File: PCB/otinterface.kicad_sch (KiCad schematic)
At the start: 43 parts, among them K1 G6K-2, Q1 BC857C, Q10 BC847C, Q11 BC857C, Q12 BC847C, Q2 BC847C, Q4 BC857C, Q5 BC857C, Q6 BC857C, Q7 BC857C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

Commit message: finish 45/24
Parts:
- K1: value G6K-2 -> G6K-2F-Y-5V; LCSC C47190 -> C2982926
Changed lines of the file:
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@@
 	(wire
 		(pts
-			(xy 193.04 88.9) (xy 220.98 88.9)
+			(xy 199.39 88.9) (xy 220.98 88.9)
 		)
 		(stroke
@@
 	(wire
 		(pts
-			(xy 193.04 92.71) (xy 175.26 92.71)
+			(xy 199.39 92.71) (xy 175.26 92.71)
 		)
 		(stroke
@@
 	(wire
 		(pts
-			(xy 193.04 88.9) (xy 193.04 92.71)
+			(xy 199.39 88.9) (xy 199.39 92.71)
 		)
 		(stroke
@@
 			)
 		)
-		(property "Value" "G6K-2"
+		(property "Value" "G6K-2F-Y-5V"
 			(at 167.64 85.09 90)
 			(effects
@@
 			)
 		)
-		(property "LCSC" "C47190"
+		(property "LCSC" "C2982926"
 			(at 167.64 102.87 0)
 			(effects

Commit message: add pullups for stability
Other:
- company: (none) -> Seegel Systeme
- title: (none) -> OT Thing
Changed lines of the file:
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@@
 	(generator_version "8.0")
 	(paper "A4")
+	(title_block
+		(title "OT Thing")
+		(date "2025-01-08")
+		(rev "2/25")
+		(company "Seegel Systeme")
+	)
 	(junction
 		(at 187.96 102.87)

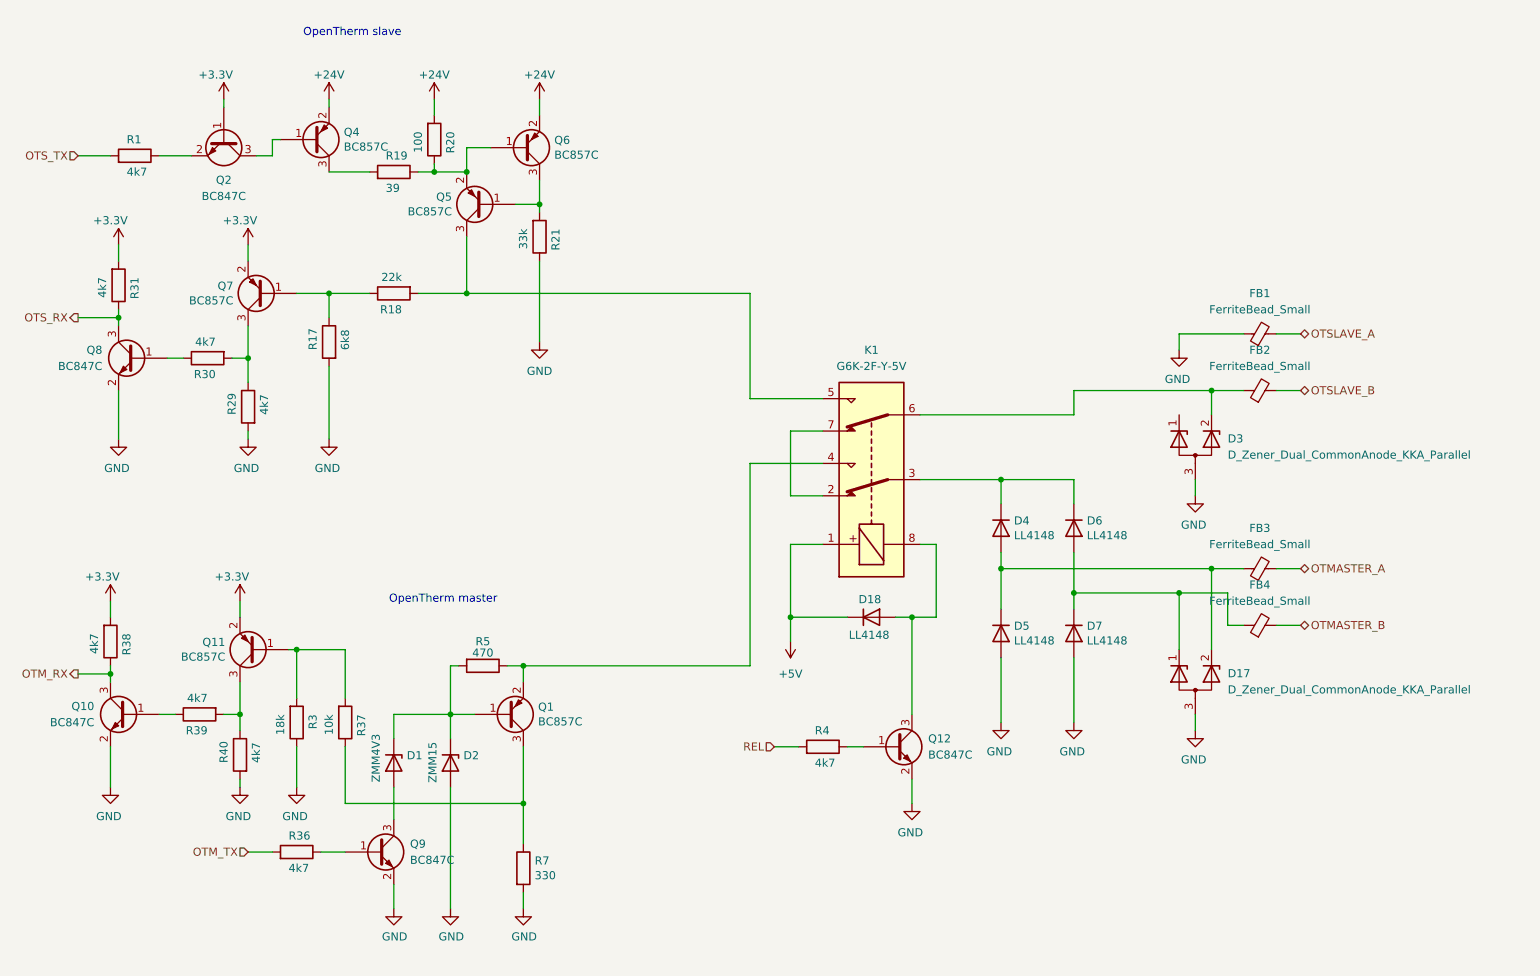
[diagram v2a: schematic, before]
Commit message: migrate to pioarduino smart power add more OT values new partitiontable
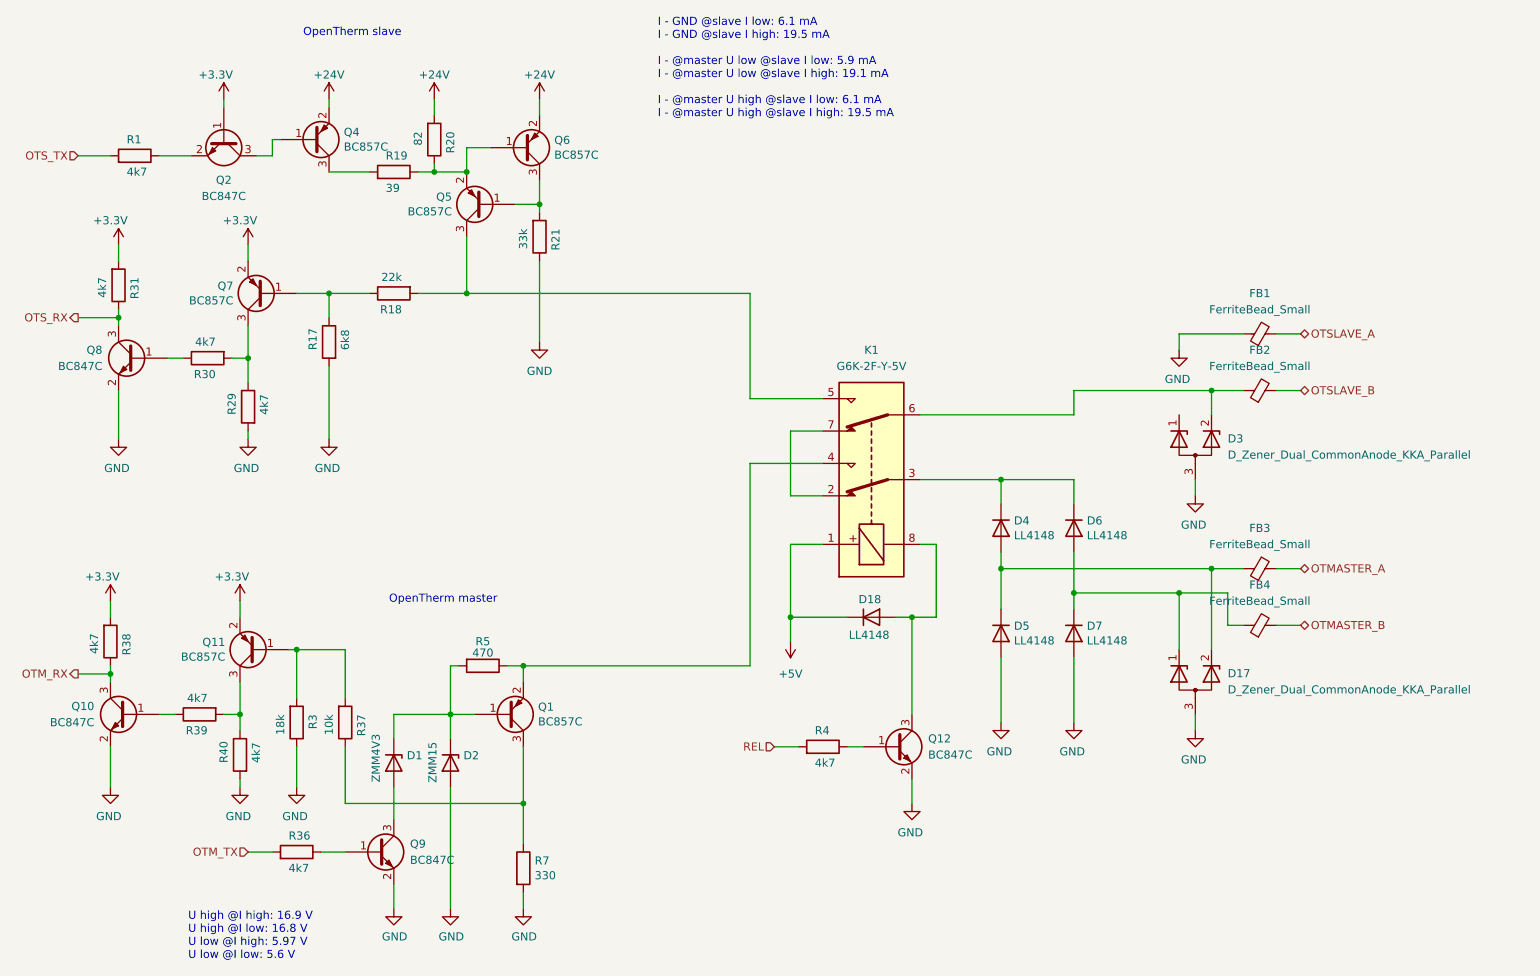
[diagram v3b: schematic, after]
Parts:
- R20: value 100 -> 82; LCSC C17408 -> C17841
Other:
- note added: "I - GND @slave I low: 6.1 mA I - GND @slave I high: 19.5 mA I - @master U low @slave I low: 5.9 mA I - @master U low @slave I high: 19.1 mA I - @master U high @slave I low: 6.1 mA I - @master U high @slave I high: 19.5 mA"
- note added: "U high @I high: 16.9 V U high @I low: 16.8 V U low @I high: 5.97 V U low @I low: 5.6 V"
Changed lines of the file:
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@@
 (kicad_sch
-	(version 20231120)
+	(version 20250114)
 	(generator "eeschema")
-	(generator_version "8.0")
+	(generator_version "9.0")
 	(paper "A4")
 	(title_block
@@
 		(company "Seegel Systeme")
 	)
+	(text "U high @I high: 16.9 V\nU high @I low: 16.8 V\nU low @I high: 5.97 V\nU low @I low: 5.6 V"
+		(exclude_from_sim no)
+		(at 60.452 174.498 0)
+		(effects
+			(font
+				(size 1.27 1.27)
+			)
+			(justify left)
+		)
+	)
+	(text "I - GND @slave I low: 6.1 mA\nI - GND @slave I high: 19.5 mA\n\nI - @master U low @slave I low: 5.9 mA\nI - @master U low @slave I high: 19.1 mA\n\nI - @master U high @slave I low: 6.1 mA\nI - @master U high @slave I high: 19.5 mA"
+		(exclude_from_sim no)
+		(at 134.112 38.354 0)
+		(effects
+			(font
+				(size 1.27 1.27)
+			)
+			(justify left)
+		)
+	)
+	(text "OpenTherm slave"
+		(exclude_from_sim no)
+		(at 78.486 33.528 0)
+		(effects
+			(font
+				(size 1.27 1.27)
+			)
+			(justify left bottom)
+		)
+	)
+	(text "OpenTherm master"
+		(exclude_from_sim no)
+		(at 91.948 122.428 0)
+		(effects
+			(font
+				(size 1.27 1.27)
+			)
+			(justify left bottom)
+		)
+	)
 	(junction
 		(at 187.96 102.87)
@@
 		)
 	)
-	(text "OpenTherm slave"
-		(exclude_from_sim no)
-		(at 78.486 33.528 0)
-		(effects
-			(font
-				(size 1.27 1.27)
-			)
-			(justify left bottom)
-		)
-	)
-	(text "OpenTherm master"
-		(exclude_from_sim no)
-		(at 91.948 122.428 0)
-		(effects
-			(font
-				(size 1.27 1.27)
-			)
-			(justify left bottom)
-		)
-	)
 	(hierarchical_label "OTS_TX"
 		(shape input)
 		(at 43.18 52.07 180)
-		(fields_autoplaced yes)
 		(effects
 			(font
@@
 		(shape output)
 		(at 43.18 133.35 180)
-		(fields_autoplaced yes)
 		(effects
 			(font
@@
 		(shape input)
 		(at 69.85 161.29 180)
-		(fields_autoplaced yes)
 		(effects
 			(font
@@
 		(shape bidirectional)
 		(at 234.95 88.9 0)
-		(fields_autoplaced yes)
 		(effects
 			(font
@@
 		(shape bidirectional)
 		(at 234.95 125.73 0)
-		(fields_autoplaced yes)
 		(effects
 			(font
@@
 		(shape input)
 		(at 152.4 144.78 180)
-		(fields_autoplaced yes)
 		(effects
 			(font
@@
 		(shape bidirectional)
 		(at 234.95 116.84 0)
-		(fields_autoplaced yes)
 		(effects
 			(font
@@
 		(shape output)
 		(at 43.18 77.47 180)
-		(fields_autoplaced yes)
 		(effects
 			(font
@@
 		(shape bidirectional)
 		(at 234.95 80.01 0)
-		(fields_autoplaced yes)
 		(effects
 			(font
@@
 			)
 		)
-		(property "Value" "100"
+		(property "Value" "82"
 			(at 96.52 48.26 90)
 			(effects
@@
 			)
 		)
-		(property "LCSC" "C17408"
+		(property "LCSC" "C17841"
 			(at 99.06 49.53 0)
 			(effects

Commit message: Migrate to KiCad 9.0
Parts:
- R20: value 82 -> 100; LCSC C17841 -> C17408
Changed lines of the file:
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@@
 			)
 		)
-		(property "Value" "82"
+		(property "Value" "100"
 			(at 96.52 48.26 90)
 			(effects
@@
 			)
 		)
-		(property "LCSC" "C17841"
+		(property "LCSC" "C17408"
 			(at 99.06 49.53 0)
 			(effects

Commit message: new production
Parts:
- D17, D3: LCSC C2831523 -> C550124
- FB1, FB2, FB3, FB4: LCSC C139168 -> C1002
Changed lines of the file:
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@@
 			)
 		)
-		(property "LCSC" "C139168"
+		(property "LCSC" "C1002"
 			(at 228.6 125.73 0)
 			(effects
@@
 			)
 		)
-		(property "LCSC" "C139168"
+		(property "LCSC" "C1002"
 			(at 228.6 80.01 0)
 			(effects
@@
 			)
 		)
-		(property "Datasheet" "~"
+		(property "Datasheet" "BZB84-C24,215"
 			(at 218.44 99.06 0)
 			(effects
@@
 			)
 		)
-		(property "LCSC" "C2831523"
+		(property "LCSC" "C550124"
 			(at 218.44 97.79 0)
 			(effects
@@
 			)
 		)
-		(property "Datasheet" "~"
+		(property "Datasheet" "BZB84-C24,215"
 			(at 218.44 135.89 0)
 			(effects
@@
 			)
 		)
-		(property "LCSC" "C2831523"
+		(property "LCSC" "C550124"
 			(at 218.44 134.62 0)
 			(effects
@@
 			)
 		)
-		(property "LCSC" "C139168"
+		(property "LCSC" "C1002"
 			(at 228.6 88.9 0)
 			(effects
@@
 			)
 		)
-		(property "LCSC" "C139168"
+		(property "LCSC" "C1002"
 			(at 228.6 116.84 0)
 			(effects

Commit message: change TVS diodes
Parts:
- removed D17, D3: D_Zener_Dual_CommonAnode_KKA_Parallel, Package_TO_SOT_SMD:SOT-23, symbol Device:D_Zener_Dual_CommonAnode_KKA_Parallel
- added D15: D_TVS, Diode_SMD:D_SOD-123, symbol Device:D_TVS
- added D16: D_Schottky, Diode_SMD:D_SOD-123, symbol Device:D_Zener
- D18, D4, D5, D6, D7: value LL4148 -> 1N4148W; footprint Diode_SMD:D_MiniMELF -> Diode_SMD:D_SOD-123; LCSC C435829 -> (none)
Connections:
- net GND: now also D16.2 (A)
- net at D6.2 (A), D7.1 (K), FB4.1: now also D15.1 (A1)
- net at D4.2 (A), D5.1 (K), FB3.1: now also D15.2 (A2)
- net at FB2.1, K1.6: now also D16.1 (K)
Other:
- moved on the sheet: FB4

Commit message: Fix ERCs, DRCs & BOM
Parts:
- D15: value D_TVS -> PESD24VL1BA; footprint Diode_SMD:D_SOD-123 -> Diode_SMD:D_SOD-323; LCSC (none) -> C2687132
- D16: value D_Schottky -> PTVS24VS1UR; LCSC (none) -> C5380693
- D18, D4, D5, D6, D7: value 1N4148W -> LL4148; footprint Diode_SMD:D_SOD-123 -> Diode_SMD:D_MiniMELF; LCSC (none) -> C435829
- FB1, FB2, FB3, FB4: value FerriteBead_Small -> ~
